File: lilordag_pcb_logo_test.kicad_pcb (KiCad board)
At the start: 2 copper layers, 98.1 x 100 mm, 134 parts, among them J1 USB4105-GF-A, Q1 BC846, Q2 BC846, Q3 MMBT3906, Q4 MMBT3906, Q5 BC846, Q6 BC846, Q7 SSM3J56MFV, Q8 SSM3J56MFV, SW1 PCM12SMTR, SW2 PCM12SMTR, U1 ESP32-C3-WROOM-02-N4

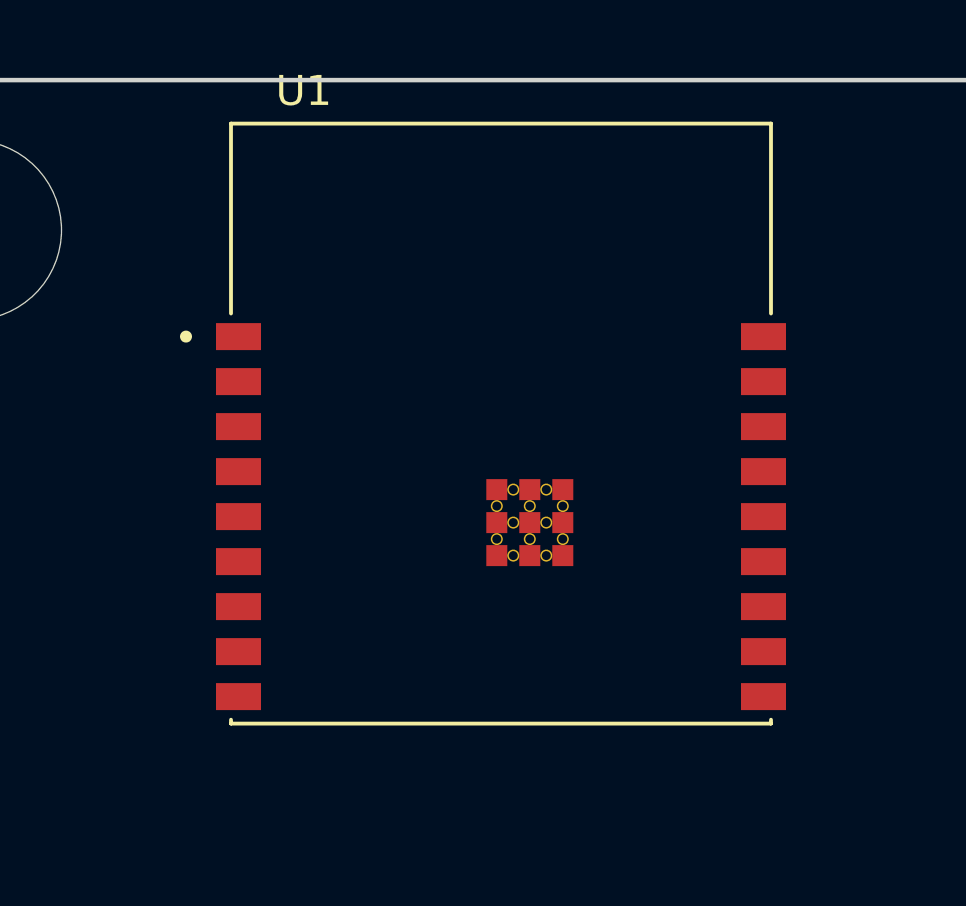
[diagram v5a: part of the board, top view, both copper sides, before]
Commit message: Downloaded assets for the esp32-c3-mini.
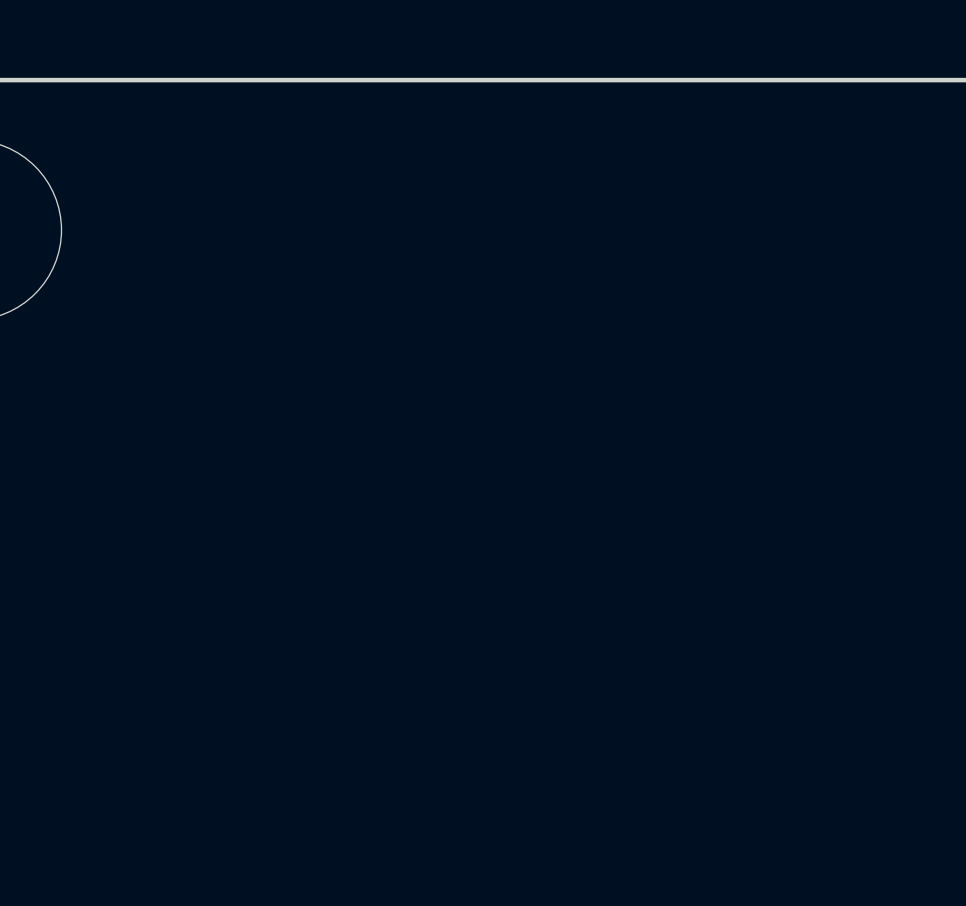
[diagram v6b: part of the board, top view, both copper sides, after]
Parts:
- removed U1: ESP32-C3-WROOM-02-N4, ESP32-C3-WROOM:MODULE_ESP32-C3-WROOM-02-H4

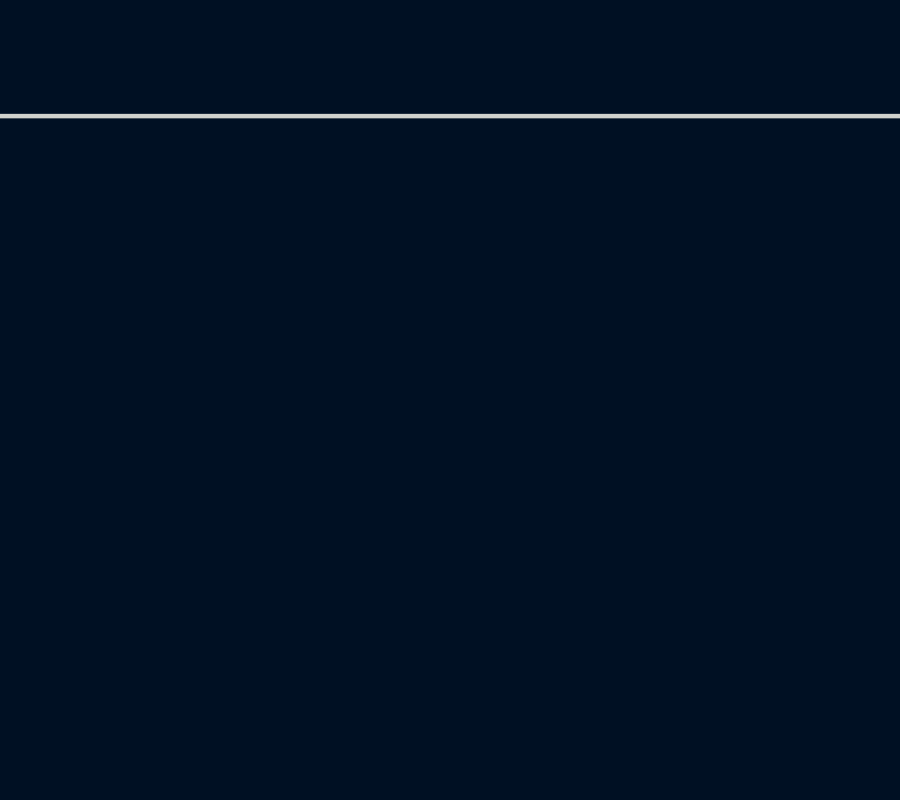
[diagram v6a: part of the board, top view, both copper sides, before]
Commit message: Added esp32c3mini to the schematic and the pcb.
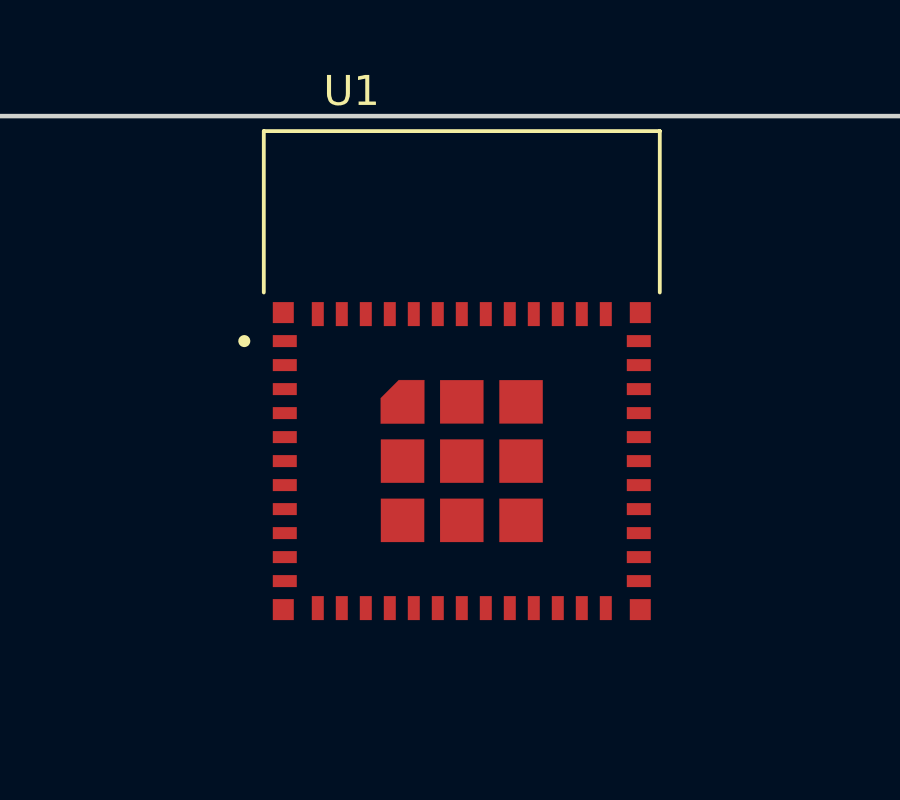
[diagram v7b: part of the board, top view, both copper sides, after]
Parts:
- added U1: ESP32-C3-MINI-1-N4, ESP32-C3-MINI:XCVR_ESP32-C3-MINI-1-N4, F.Cu at (51.4, 38.8)

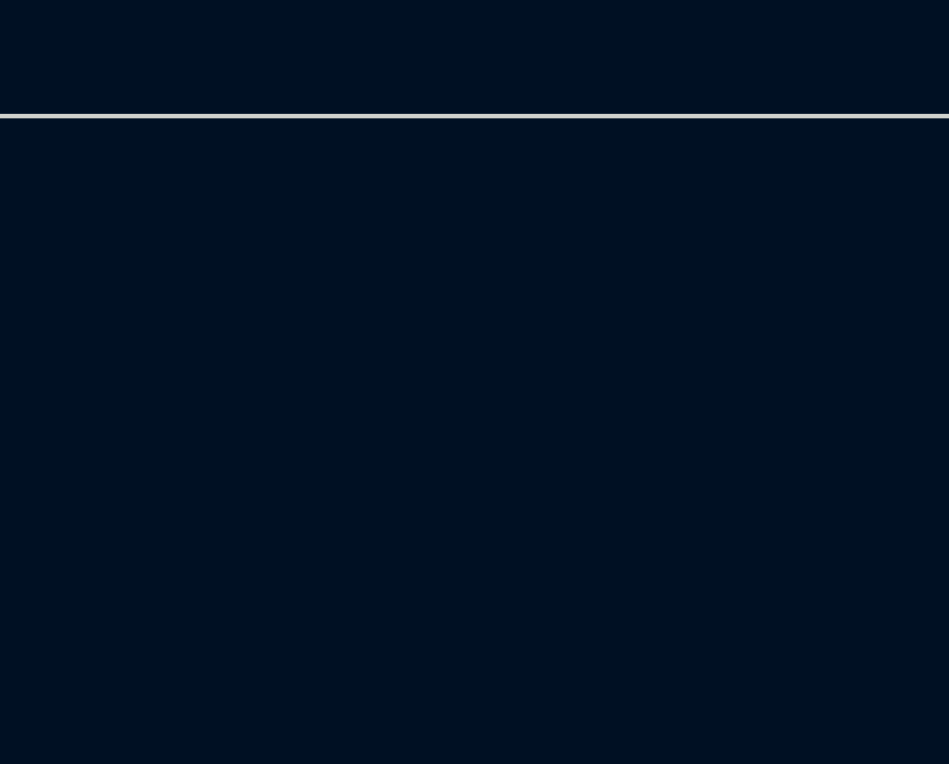
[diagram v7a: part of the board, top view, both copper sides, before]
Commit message: Added reset button for the ESP.
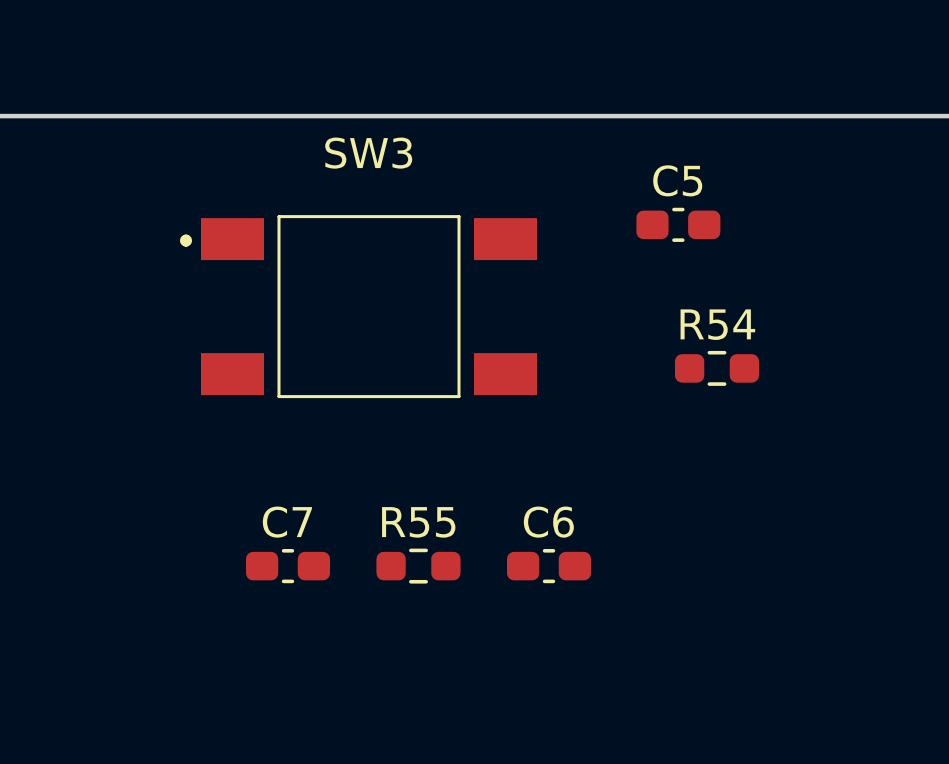
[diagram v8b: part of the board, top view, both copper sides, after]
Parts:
- added C5: 1uf, Capacitor_SMD:C_0603_1608Metric_Pad1.08x0.95mm_HandSolder, F.Cu at (86.6, 33.6)
- added C6: 10nF, Capacitor_SMD:C_0603_1608Metric_Pad1.08x0.95mm_HandSolder, F.Cu at (82.3, 45.0)
- added C7: 0.1nF, Capacitor_SMD:C_0603_1608Metric_Pad1.08x0.95mm_HandSolder, F.Cu at (73.6, 45.0)
- added R54: 10k, Resistor_SMD:R_0603_1608Metric_Pad0.98x0.95mm_HandSolder, F.Cu at (87.9, 38.4)
- added R55: 10k, Resistor_SMD:R_0603_1608Metric_Pad0.98x0.95mm_HandSolder, F.Cu at (77.9, 45.0)
- added SW3: SW_MEC_5G, switch-TL3301AF260QG:TL3301AF260QG, F.Cu at (76.3, 36.4)
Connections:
- U1 pad 1: Net-(U1-Pad1) -> GND
- U1 pad 11: Net-(U1-Pad1) -> GND
- U1 pad 14: Net-(U1-Pad1) -> GND
- U1 pad 2: Net-(U1-Pad1) -> GND
- U1 pad 3: unconnected-(U1-Pad3) -> +3.3V
- U1 pad 36: Net-(U1-Pad1) -> GND
- U1 pad 37: Net-(U1-Pad1) -> GND
- U1 pad 38: Net-(U1-Pad1) -> GND
- U1 pad 39: Net-(U1-Pad1) -> GND
- U1 pad 40: Net-(U1-Pad1) -> GND
- U1 pad 41: Net-(U1-Pad1) -> GND
- U1 pad 42: Net-(U1-Pad1) -> GND
- U1 pad 43: Net-(U1-Pad1) -> GND
- U1 pad 44: Net-(U1-Pad1) -> GND
- U1 pad 45: Net-(U1-Pad1) -> GND
- U1 pad 46: Net-(U1-Pad1) -> GND
- U1 pad 47: Net-(U1-Pad1) -> GND
- U1 pad 48: Net-(U1-Pad1) -> GND
- U1 pad 49_1: Net-(U1-Pad1) -> GND
- U1 pad 49_2: Net-(U1-Pad1) -> GND
- U1 pad 49_3: Net-(U1-Pad1) -> GND
- U1 pad 49_4: Net-(U1-Pad1) -> GND
- U1 pad 49_5: Net-(U1-Pad1) -> GND
- U1 pad 49_6: Net-(U1-Pad1) -> GND
- U1 pad 49_7: Net-(U1-Pad1) -> GND
- U1 pad 49_8: Net-(U1-Pad1) -> GND
- U1 pad 49_9: Net-(U1-Pad1) -> GND
- U1 pad 5: unconnected-(U1-Pad5) -> Net-(U1-Pad5)
- U1 pad 50: Net-(U1-Pad1) -> GND
- U1 pad 51: Net-(U1-Pad1) -> GND
- U1 pad 52: Net-(U1-Pad1) -> GND
- U1 pad 53: Net-(U1-Pad1) -> GND
- U1 pad 8: unconnected-(U1-Pad8) -> ENABLE
